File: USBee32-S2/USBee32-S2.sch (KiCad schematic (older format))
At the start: 45 parts, among them IC1 IP4220CZ6, J1 USB_A, J2 TYPE-C-31-M-12, J3 Conn_01x18_Male, J4 S2B-PH-SM4-TB(LF)(SN), J5 Conn_01x22_Male, Q1 MMBT8050, Q2 MMBT8050, SW1 SW_Push, SW2 SW_Push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

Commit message: Made suggested routing, placement changes
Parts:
- J4: footprint S2B-PH-SM4-TB_LF_SN:JST_S2B-PH-SM4-TB(LF)(SN) -> Connector_JST:JST_PH_B2B-PH-SM4-TB_1x02-1MP_P2.00mm_Vertical
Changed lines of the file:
@@
 F 0 "J4" V 5890 4840 50  0000 R CNN
 F 1 "S2B-PH-SM4-TB(LF)(SN)" V 5790 5135 50  0000 R CNN
-F 2 "S2B-PH-SM4-TB_LF_SN:JST_S2B-PH-SM4-TB(LF)(SN)" H 5535 4790 50  0001 L BNN
+F 2 "Connector_JST:JST_PH_B2B-PH-SM4-TB_1x02-1MP_P2.00mm_Vertical" H 5535 4790 50  0001 L BNN
 F 3 "" H 5535 4790 50  0001 L BNN
 F 4 "Manufacturer Recommendation" H 5535 4790 50  0001 L BNN "STANDARD"

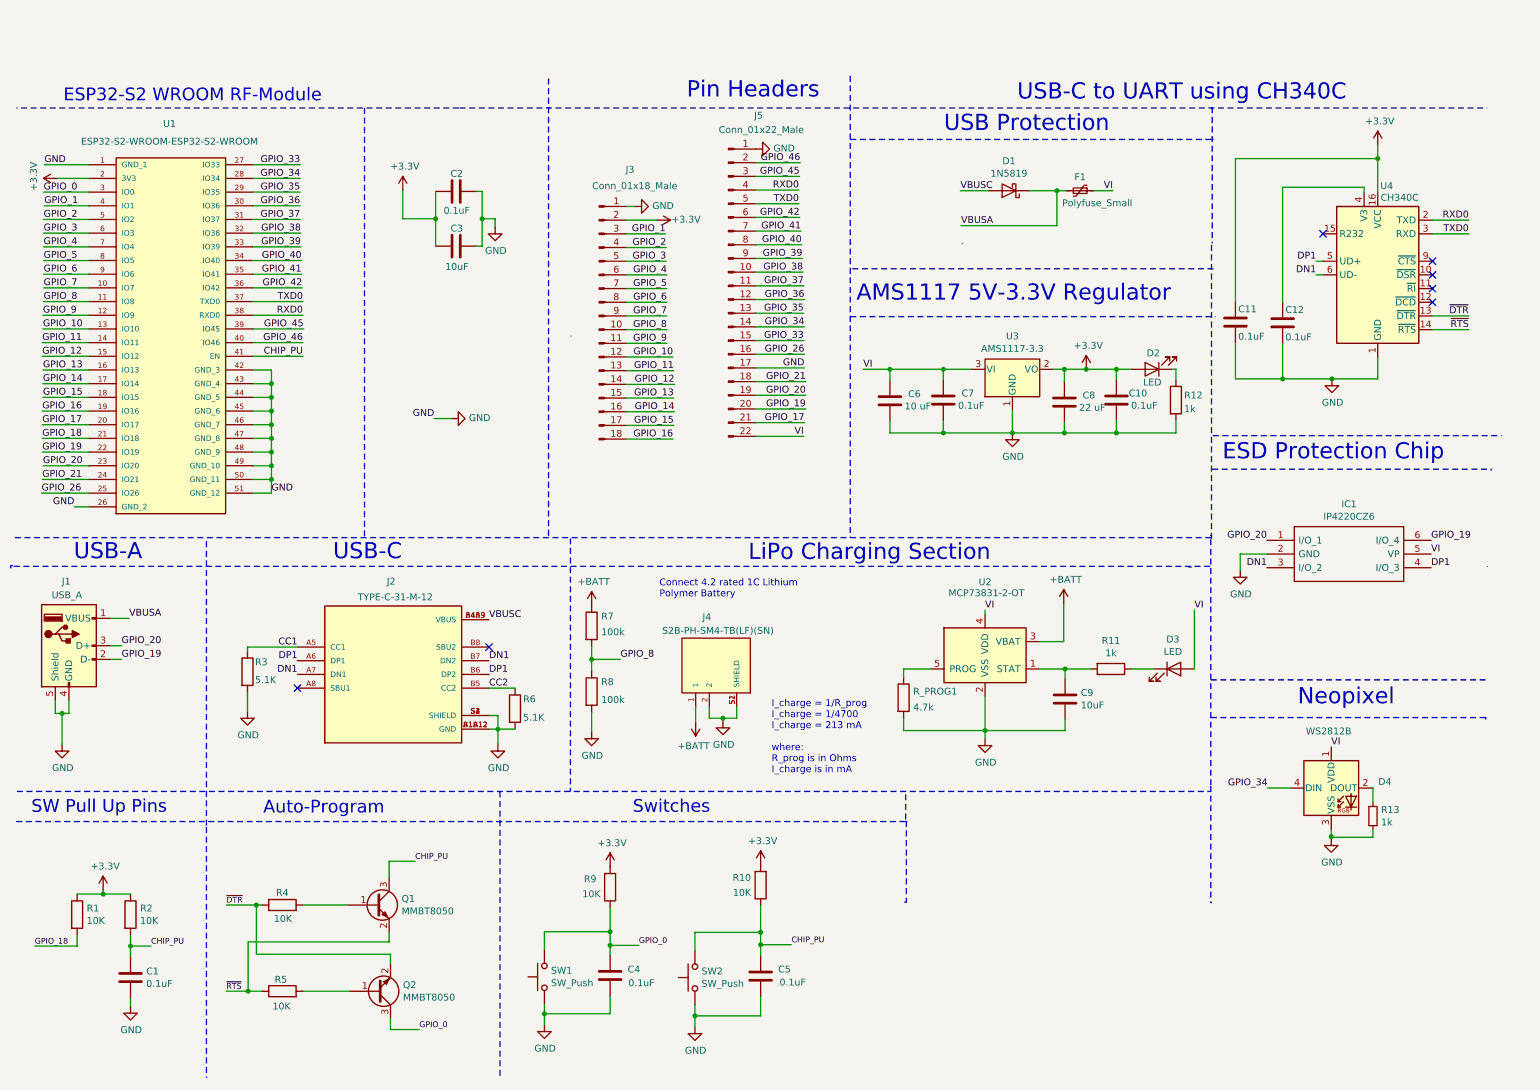
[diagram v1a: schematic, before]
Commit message: Completed routing 4-layer board
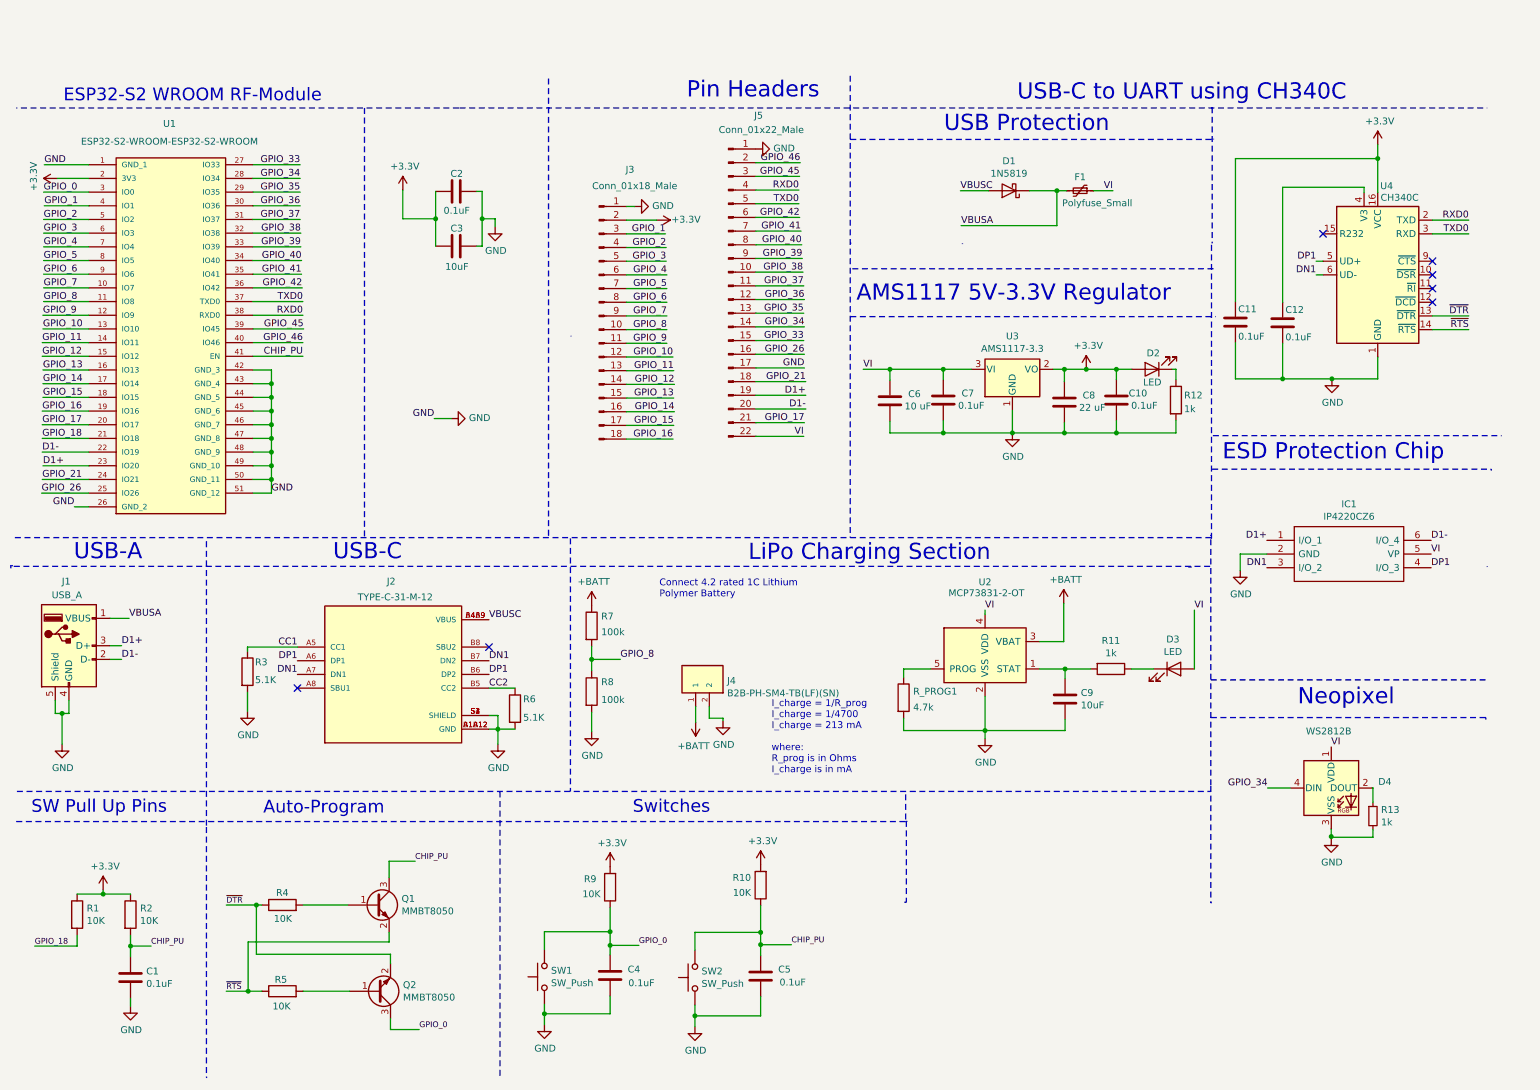
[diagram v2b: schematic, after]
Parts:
- removed J4: S2B-PH-SM4-TB(LF)(SN), Connector_JST:JST_PH_B2B-PH-SM4-TB_1x02-1MP_P2.00mm_Vertical, symbol S2B-PH-SM4-TB_LF__SN_:S2B-PH-SM4-TB(LF)(SN)
- added J4: B2B-PH-SM4-TB(LF)(SN), B2B-PH-SM4-TB:JST_B2B-PH-SM4-TB(LF)(SN), symbol B2B-PH-SM4-TB_LF__SN_:B2B-PH-SM4-TB(LF)(SN)
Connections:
- net +BATT: now also J4.1
- net GND: now also J4.2
- net GPIO_19 renamed D1-
- net GPIO_20 renamed D1+
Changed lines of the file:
@@
 GPIO_17
 Text Label 660  3230 0    50   ~ 0
-GPIO_19
+D1-
 Text Label 665  3330 0    50   ~ 0
-GPIO_20
+D1+
 Text Label 660  3430 0    50   ~ 0
 GPIO_21
@@
 $EndComp
 Text Label 1240 4645 0    50   ~ 0
-GPIO_20
+D1+
 Text Label 1240 4745 0    50   ~ 0
-GPIO_19
+D1-
 Text Label 5215 1635 2    50   ~ 0
 GPIO_1
@@
 GPIO_21
 Text Label 6240 2815 2    50   ~ 0
-GPIO_20
+D1+
 Wire Wire Line
 	5875 2715 6240 2715
@@
 $EndComp
 Text Label 6240 2915 2    50   ~ 0
-GPIO_19
+D1-
 Wire Wire Line
 	5875 2915 6240 2915
@@
 $EndComp
 Text Label 9610 3875 2    50   ~ 0
-GPIO_20
+D1+
 $Comp
 L IP4220CZ6:IP4220CZ6 IC1
@@
 	1    0    0    -1
 $EndComp
-Text Label 10810 3875 0    50   ~ 0
-GPIO_19
 Text Label 9610 4075 2    50   ~ 0
 DN1
@@
 $EndComp
 $Comp
-L S2B-PH-SM4-TB_LF__SN_:S2B-PH-SM4-TB(LF)(SN) J4
-U 1 1 60A6168B
-P 5535 4790
-F 0 "J4" V 5890 4840 50  0000 R CNN
-F 1 "S2B-PH-SM4-TB(LF)(SN)" V 5790 5135 50  0000 R CNN
-F 2 "Connector_JST:JST_PH_B2B-PH-SM4-TB_1x02-1MP_P2.00mm_Vertical" H 5535 4790 50  0001 L BNN
-F 3 "" H 5535 4790 50  0001 L BNN
-F 4 "Manufacturer Recommendation" H 5535 4790 50  0001 L BNN "STANDARD"
-F 5 "JST" H 5535 4790 50  0001 L BNN "MANUFACTURER"
-	1    5535 4790
-	0    -1   -1   0
-$EndComp
-$Comp
 L ESP32-S2-rescue:GND-power #PWR012
 U 1 1 60A9405E
@@
 Wire Wire Line
 	5535 5175 5635 5175
-Wire Wire Line
-	5735 5175 5735 5090
 $Comp
 L ESP32-S2-rescue:GND-power #PWR018
@@
 Wire Wire Line
 	5635 5195 5635 5175
-Connection ~ 5635 5175
-Wire Wire Line
-	5635 5175 5735 5175
 Wire Wire Line
 	7150 4815 6955 4815
@@
 Text Label 3525 2985 2    50   ~ 0
 GND
+$Comp
+L B2B-PH-SM4-TB_LF__SN_:B2B-PH-SM4-TB(LF)(SN) J4
+U 1 1 60F7770E
+P 5435 4890
+F 0 "J4" V 5424 4660 50  0000 R CNN
+F 1 "B2B-PH-SM4-TB(LF)(SN)" V 5333 4660 50  0000 R CNN
+F 2 "B2B-PH-SM4-TB:JST_B2B-PH-SM4-TB(LF)(SN)" H 5435 4890 50  0001 L BNN
+F 3 "" H 5435 4890 50  0001 L BNN
+F 4 "JST" H 5435 4890 50  0001 L BNN "MANUFACTURER"
+	1    5435 4890
+	0    -1   -1   0
+$EndComp
+Text Label 10810 3875 0    50   ~ 0
+D1-
 $EndSCHEMATC

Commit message: Routing and placement cleaned
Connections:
- net GPIO_17: now also D4.4 (DIN)
- net GPIO_34: no longer D4.4 (DIN)
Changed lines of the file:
@@
 	9215 3110 11325 3110
 Text Label 9615 5685 2    50   ~ 0
-GPIO_34
+GPIO_17
 Text Label 10080 5385 0    50   ~ 0
 VI

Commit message: Added differential pair to USB circuitry
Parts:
- renumbered R_PROG1 to R14, IC1 to U5
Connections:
- net +3V3: now also J5.17 (Pin_17)
- net GND: no longer J5.17 (Pin_17)
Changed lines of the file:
@@
 Wire Wire Line
 	8510 2625 8620 2625
-Wire Wire Line
-	5875 2615 6230 2615
-Text Label 6230 2615 2    50   ~ 0
-GND
 $Comp
 L ESP32-S2-rescue:SW_Push-Switch SW1
@@
 D1+
 $Comp
-L IP4220CZ6:IP4220CZ6 IC1
+L IP4220CZ6:IP4220CZ6 U5
 U 1 1 60A01739
 P 9610 3875
-F 0 "IC1" H 10210 4140 50  0000 C CNN
+F 0 "U5" H 10210 4140 50  0000 C CNN
 F 1 "IP4220CZ6" H 10210 4049 50  0000 C CNN
 F 2 "IP4220CZ6:SOP95P275X110-6N" H 10660 3975 50  0001 L CNN
@@
 Neopixel
 $Comp
-L ESP32-S2-rescue:R-Device R_PROG1
+L ESP32-S2-rescue:R-Device R14
 U 1 1 60A58974
 P 6955 5025
-F 0 "R_PROG1" H 7025 5071 50  0000 L CNN
+F 0 "R14" H 7025 5071 50  0000 L CNN
 F 1 "4.7k" H 7025 4955 50  0000 L CNN
 F 2 "Resistor_SMD:R_0603_1608Metric" V 6885 5025 50  0001 C CNN
@@
 Text Label 10810 3875 0    50   ~ 0
 D1-
+$Comp
+L ESP32-S2-rescue:+3.3V-power #PWR029
+U 1 1 60F17964
+P 6150 2615
+F 0 "#PWR029" H 6150 2465 50  0001 C CNN
+F 1 "+3.3V" V 6145 2830 50  0000 C CNN
+F 2 "" H 6150 2615 50  0001 C CNN
+F 3 "" H 6150 2615 50  0001 C CNN
+	1    6150 2615
+	0    1    1    0
+$EndComp
+Wire Wire Line
+	6150 2615 5875 2615
 $EndSCHEMATC

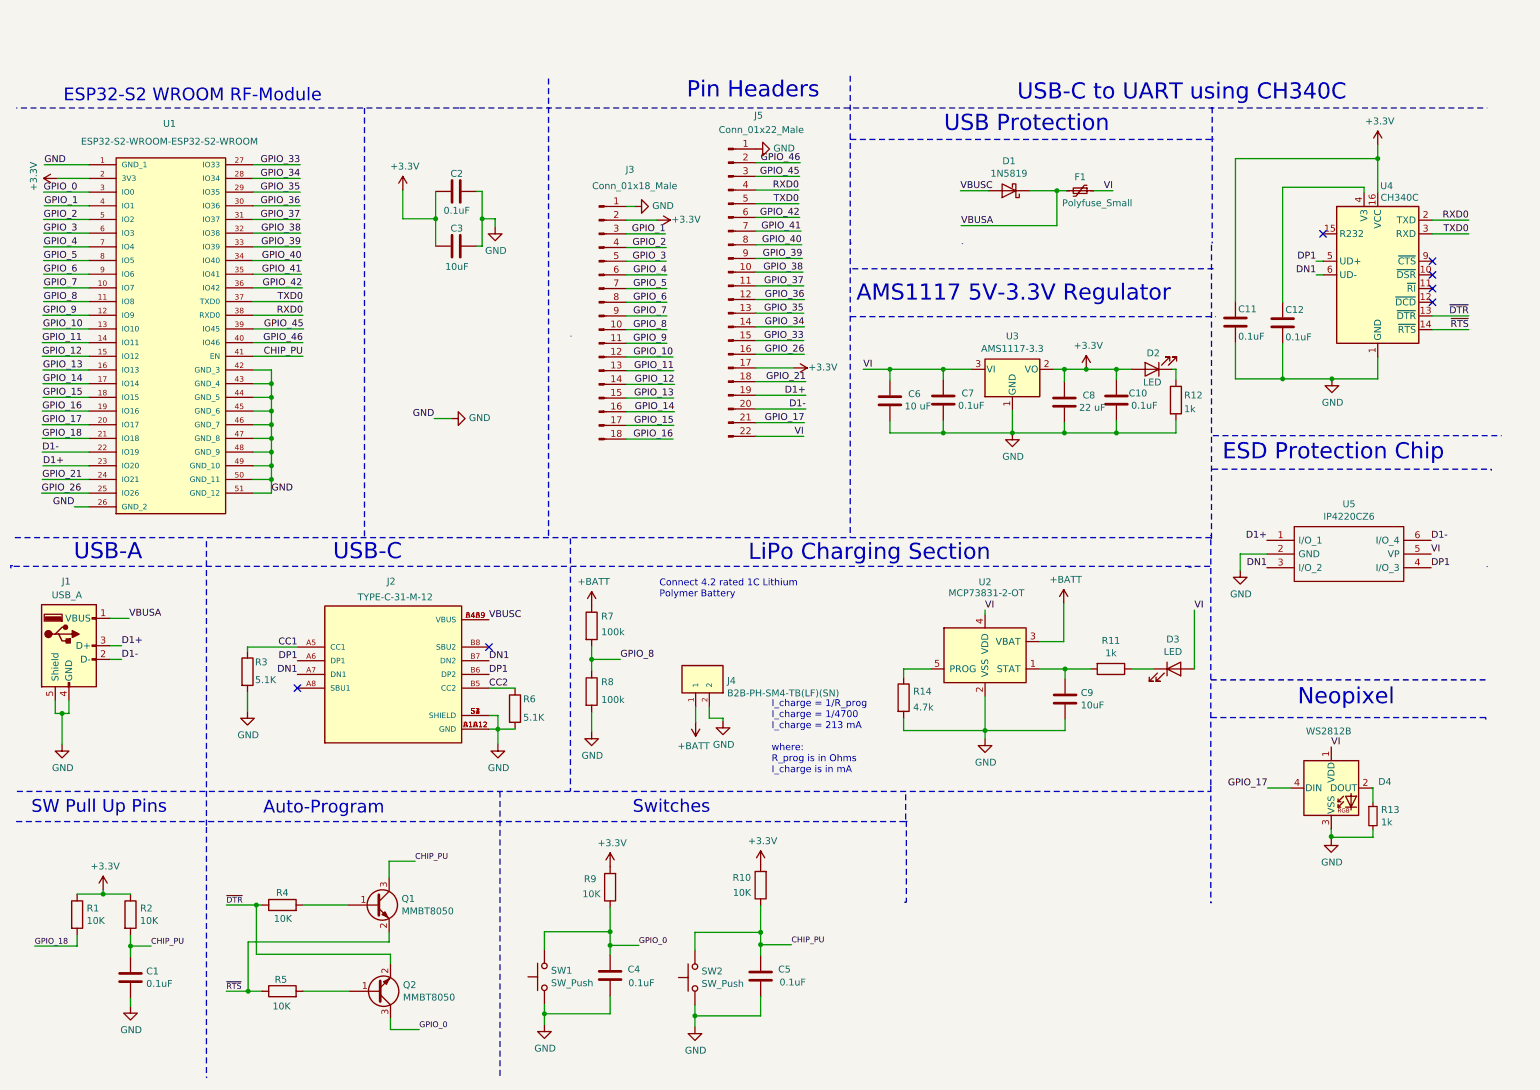
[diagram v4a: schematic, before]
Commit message: Rectified neopixel, battery charging errors, updated routing
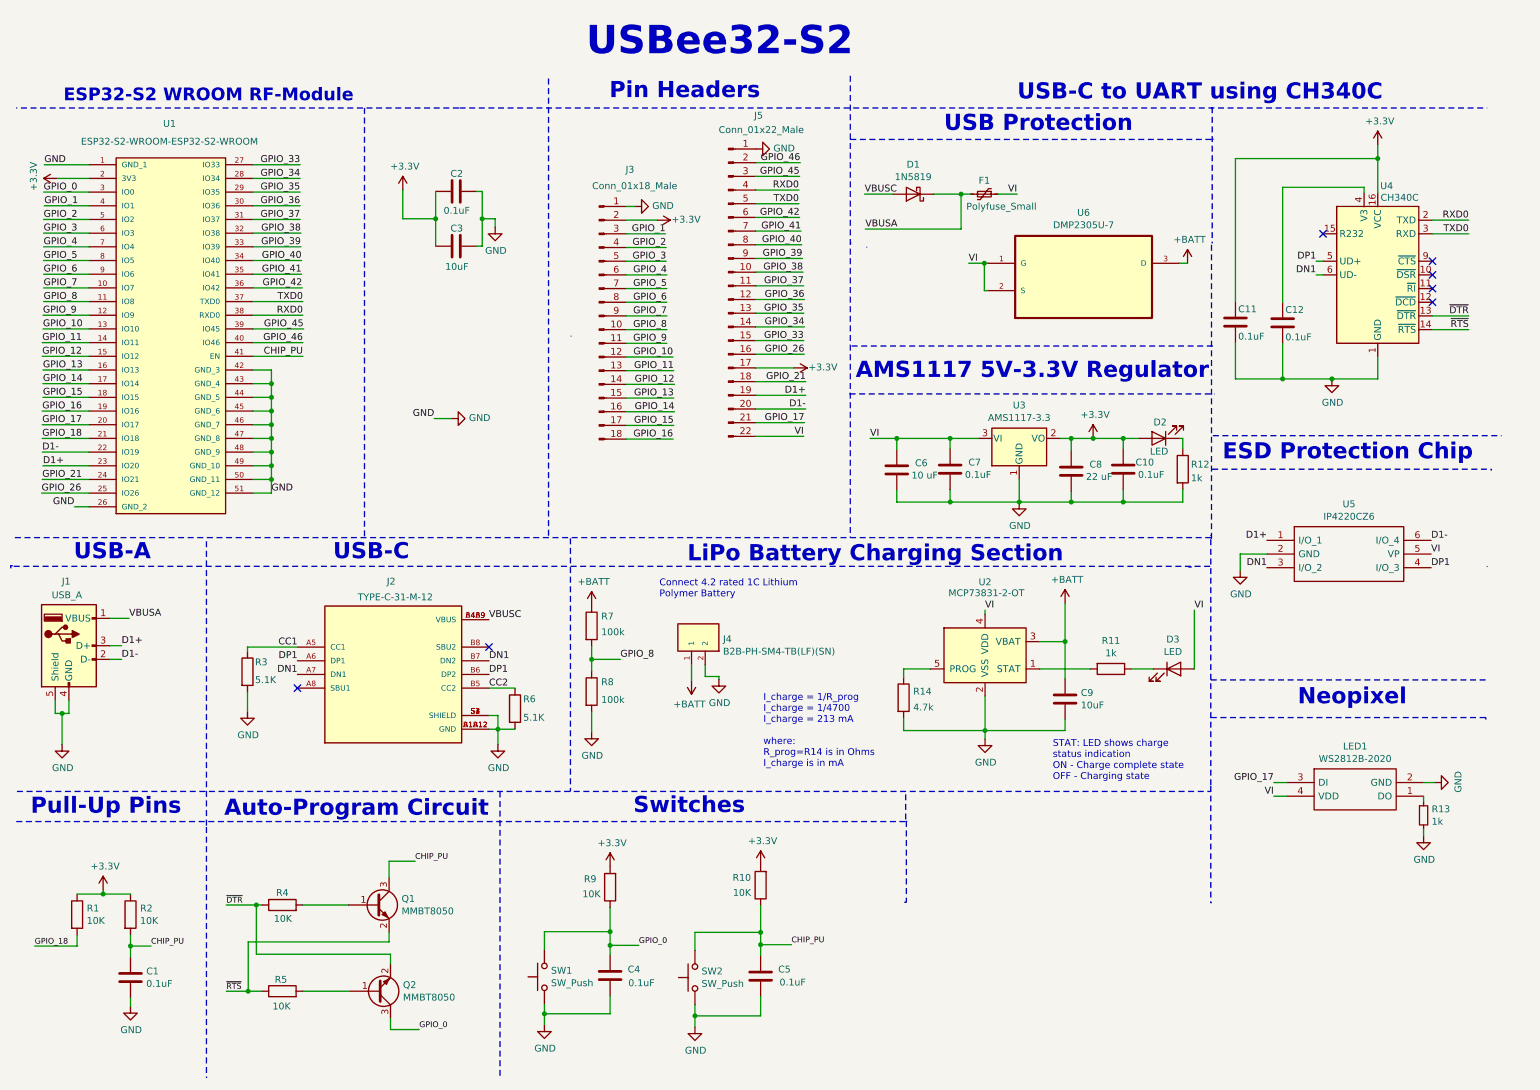
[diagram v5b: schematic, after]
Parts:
- removed D4: WS2812B, WS2018:WS2812B2020, symbol ESP32-S2-rescue:WS2812B-LED
- added LED1: WS2812B-2020, WS2812B-2020:WS2812B2020, symbol WS2812B-2020:WS2812B-2020
- added U6: DMP2305U-7, DMP2305U-7:SOT103P240X110-3N, symbol DMP2305U-7:DMP2305U-7
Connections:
- net +BATT: now also C9.1, U6.3 (D)
- net GND: now also LED1.2 (GND)
- net GPIO_17: now also LED1.3 (DI)
- net VI: now also LED1.4 (VDD), U6.1 (G), U6.2 (S)
- net at R11.2, U2.1 (STAT): no longer C9.1
- net at R13.1: now also LED1.1 (DO)
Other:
- note added: "Auto-Program Circuit\n"
- note added: "I_charge = 1/R_prog\nI_charge = 1/4700 \nI_charge = 213 mA\n \nwhere:\nR_prog=R14 is in Ohms\nI_charge is in mA"
- note added: "LiPo Battery Charging Section\n"
- note added: "Pull-Up Pins"
- note added: "STAT: LED shows charge \nstatus indication \nON - Charge complete state\nOFF - Charging state"
- note added: "USBee32-S2"
- note removed: "Auto-Program\n"
- note removed: "I_charge = 1/R_prog\nI_charge = 1/4700 \nI_charge = 213 mA\n \nwhere:\nR_prog is in Ohms\nI_charge is in mA"
- note removed: "LiPo Charging Section\n"
- note removed: "SW Pull Up Pins"
- moved on the sheet: C10, C6, C7, C8, D1, D2, F1, J4, R12, R13, U3
